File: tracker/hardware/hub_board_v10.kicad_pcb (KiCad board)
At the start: 2 copper layers, 72 x 80 mm, 28 parts, among them U1 U1, U2 U2, U3 U3, U5 U5, U6 U6, U7 U7

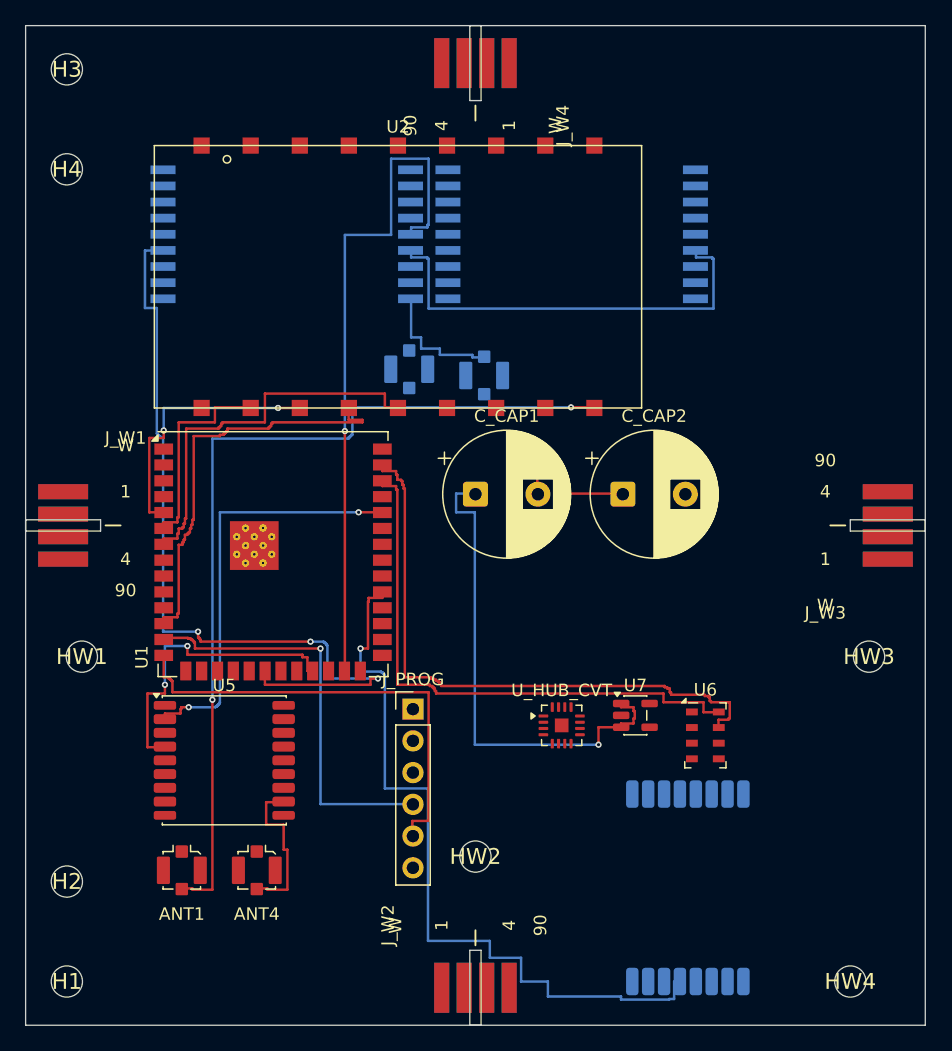
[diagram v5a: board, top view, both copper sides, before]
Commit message: fix(router): B47 -- grid marked vias 0.15mm short of the validator (consistency, NOT a win)
HONEST FRAMING: this makes the router INTERNALLY CONSISTENT. It does NOT improve the board and it
COSTS one net (19 -> 18). The board was already correct in both states -- validate_plan gates every
route, so no bad copper was ever emitted. What B47 removes is WASTED SEARCH: the grid let A* find
paths the validator then refused, which is why /U3_BUSY, /USB_DN, /GNSS_RX and /F33_RESET_N failed
with "self-check: isolation vs routed via <net> (via)" at every pitch and ordering.

THE ARITHMETIC (from validate_plan, which is the authority):
  track-vs-via  centre >= CLEAR + TRACK_W/2 + VIA_D/2 = 0.20 + 0.10 + 0.25 = 0.55mm
  via-vs-via    centre >= CLEAR + VIA_D/2   + VIA_D/2 = 0.20 + 0.25 + 0.25 = 0.70mm
Both grid-marking sites used the TRACK figure, so vias were marked 0.15mm short for the via-vs-via
case. Now marked at max(0.55, 0.70) = 0.70, so the grid can never permit what the validator refuses.
Same shape as B34/B37/B40: the grid was less strict than the check.

COST, STATED PLAINLY: a stricter grid removes detour options, so pass 2 recovered 4 nets instead of
5. 18 nets / 451 tracks / 16 vias, 9/9 custom gates rc=0, kicad-cli DRC rc=0 (0 failing,
103 unconnected). Track count rose 371 -> 451 for fewer nets because the paths now detour further.
Kept because a router whose search and validator disagree is the exact bug class that produced B34,
B37, B38, B40, B44 and B46 -- and because the discarded work made every pitch/ordering sweep
untrustworthy as a CAPACITY measurement, which is the measurement the two-layer decision needs.
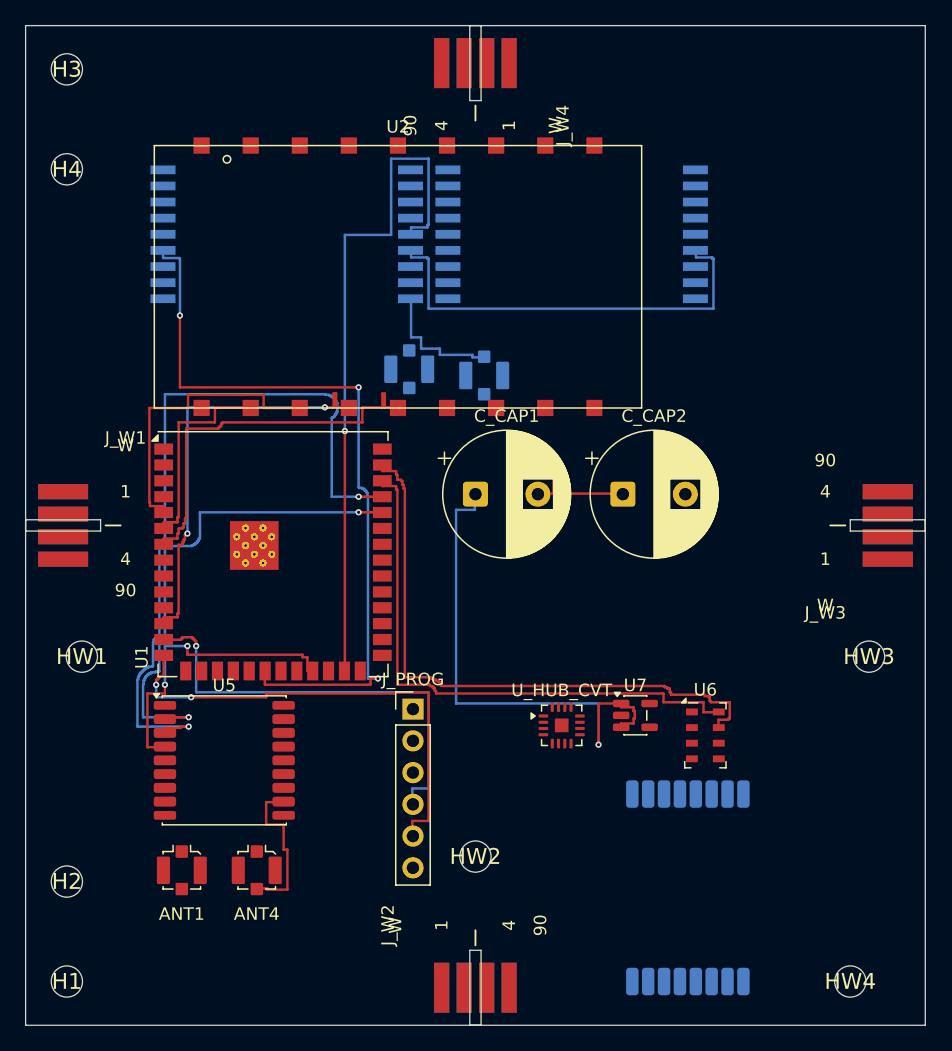
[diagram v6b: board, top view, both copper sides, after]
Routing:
- net /ANT1_433_TX: track 71.7 -> 0.00 mm, vias 2 -> 0
- net /GNSS_RX: track 0.00 -> 61.8 mm, vias 0 -> 2
- net /E28_BUSY: track 61.4 -> 0.00 mm, vias 1 -> 0
- net /GNSS_TX: track 33.9 -> 41.2 mm
- net /U3_CS_N: track 65.0 -> 62.1 mm
- net /USB_DN: track 33.4 -> 36.1 mm
- net /SPI2_MOSI: track 21.6 -> 23.7 mm, vias 2 -> 0
- net /USB_DP: track 37.0 -> 39.0 mm, vias 0 -> 2
- net /VSCAP: track 40.3 -> 42.2 mm
- net /F33_BUSY: vias 0 -> 2

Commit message: feat(v10): ADR-129 landed -- 25 refs in schematic AND board, 11/11 gates green, 3D renders ready
VERIFIED BY THE MANAGER, not relayed from the worker's self-report:
  footprints 28 -> 53 (45 parts + 8 holes); all 25 new refs present, none missing
  11/11 gates rc=0: 7 lane gates + hole_clearance + board_geometry + check_drc + schematic_parity
  check_schematic_parity  G1..G5 PASS, 58 nets agree BOTH ways, per-net pin sets equal
  kicad-cli DRC  0 failing violations (16 copper_edge_clearance + 152 silk_overlap + 28
    silk_over_copper, all three pre-existing and scoped-allowed)
  ERC 21 -> 11 errors (7 label_dangling + 2 pin_not_driven + 2 power_pin_not_driven)
  min_through_hole_diameter 0.2 preserved in the canonical .kicad_pro
  board TRACKS = 0 -- the worker did NOT route, per ADR-120 R3

TWO DEFECTS FOUND AND FIXED AFTER THE WORKER'S REPORT, both mine to catch:
1. silk_edge_clearance (NEW class, 1 item) -- "Reference field of J_HUB_PV" at x=69.0 on a 72.0mm
   board. The worker reported DRC clean but its own build introduced this. My FIRST fix GUESSED the
   text width from a per-character estimate and did not fire at all; the measured bounding box was
   (65.26,60.77)-(72.74,62.47), i.e. 0.74mm past the edge. Corrected to use
   GetBoundingBox() and shift by the MEASURED overhang -- now a general builder rule with a
   0.30mm silk-to-edge margin, so no future part can repeat it. This matters electrically only as
   assembly readability, but it is a DRC failure and DRC is the authority.
2. The ERC allowance was still 17 label_dangling after only 7 remained. An inflated allowance masks
   a regression exactly like a gate that cannot fail, so it is TIGHTENED to the measured 7 with the
   remaining seven NAMED in-source. A new dangling label now changes the count and fails the gate.

ADR-129 CLOSED TEN OF SEVENTEEN DANGLING NETS, measured:
  /F33_VCC 1->5  /GNSS_VCC 1->3  /HUB_PV_P 1->3  /HUB_PV_N 1->3  /W1_SOLAR_P 1->3
  /F33_VSENSE 1->4  /CUT_SENSE_W1..W4 1->2 e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
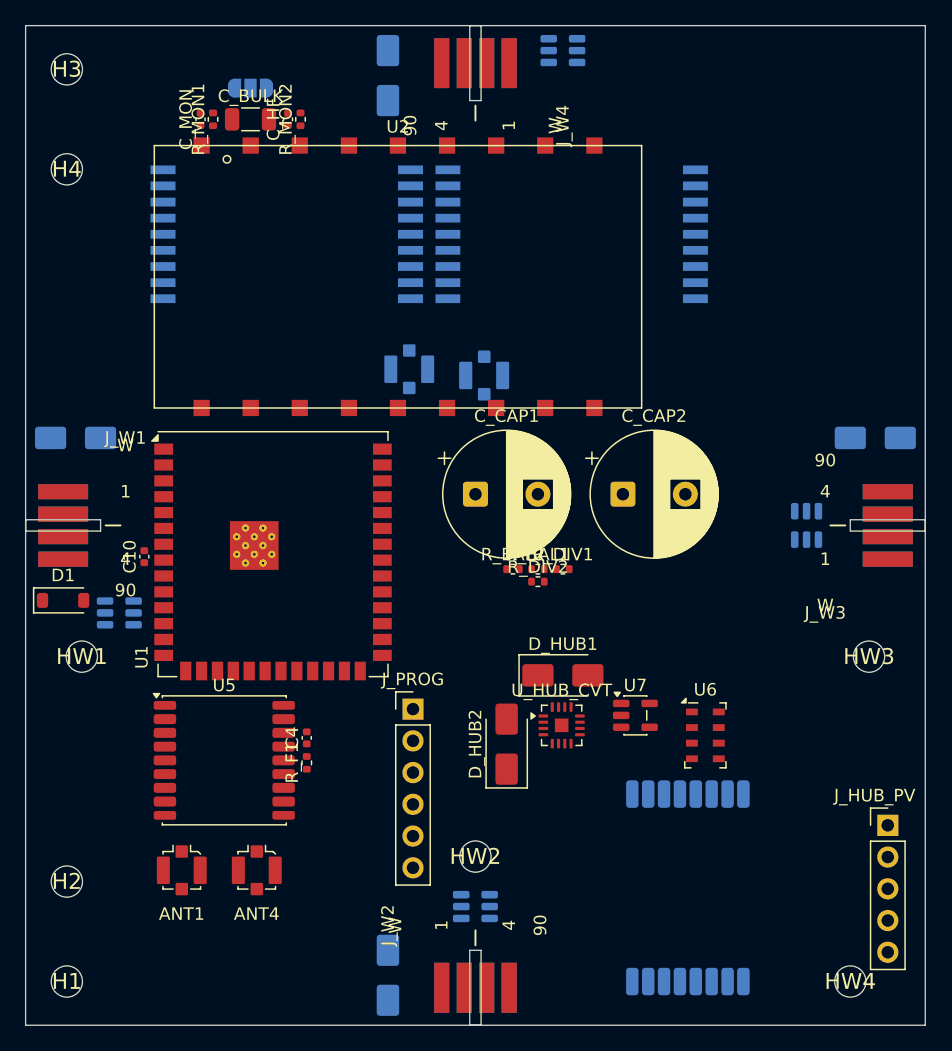
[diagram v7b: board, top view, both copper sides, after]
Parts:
- added C10: 10uF, C_0402_1005Metric, F.Cu at (9.50, 42.5)
- added C4: 10uF, C_0402_1005Metric, F.Cu at (22.5, 57.0)
- added C_BULK: 100uF, C_1206_3216Metric, F.Cu at (18.0, 7.50)
- added C_HF: 100nF, C_0402_1005Metric, F.Cu at (21.0, 7.50)
- added C_MON: 10nF, C_0402_1005Metric, F.Cu at (14.0, 7.50)
- added D1: BAT54, D_SOD-123, F.Cu at (3.00, 46.0)
- added D_BP1: SS24, D_SMA, B.Cu at (4.00, 33.0)
- added D_BP2: SS24, D_SMA, B.Cu at (29.0, 76.0)
- added D_BP3: SS24, D_SMA, B.Cu at (68.0, 33.0)
- added D_BP4: SS24, D_SMA, B.Cu at (29.0, 4.00)
- added D_HUB1: SS24, D_SMA, F.Cu at (43.0, 52.0)
- added D_HUB2: SS24, D_SMA, F.Cu at (38.5, 57.5)
- added J_HUB_PV: HUB_PV_PANEL_5P (P | MID1 | spare | N | GND), PinHeader_1x05_P2.54mm_Vertical, F.Cu at (69.0, 64.0)
- added J_VCC: F33_VCC_SEL (VSCAP | +3V3), SolderJumper-3_P1.3mm_Open_RoundedPad1.0x1.5mm, B.Cu at (18.0, 5.00)
- added R_BAL1: 10k, R_0402_1005Metric, F.Cu at (41.0, 43.5)
- added R_BAL2: 10k, R_0402_1005Metric, F.Cu at (39.0, 43.5)
- added R_DIV1: 1M, R_0402_1005Metric, F.Cu at (43.0, 43.5)
- added R_DIV2: 1M, R_0402_1005Metric, F.Cu at (41.0, 44.5)
- added R_F1: 100R, R_0402_1005Metric, F.Cu at (22.5, 59.0)
- added R_MON1: 4.7M, R_0402_1005Metric, F.Cu at (15.0, 7.50)
- added R_MON2: 4.7M, R_0402_1005Metric, F.Cu at (22.0, 7.50)
- added U_CUT1: latched cut driver + cut-sense (part TODO(unverified)), SOT-23-6, B.Cu at (7.50, 47.0)
- added U_CUT2: latched cut driver + cut-sense (part TODO(unverified)), SOT-23-6, B.Cu at (36.0, 70.5)
- added U_CUT3: latched cut driver + cut-sense (part TODO(unverified)), SOT-23-6, B.Cu at (62.5, 40.0)
- added U_CUT4: latched cut driver + cut-sense (part TODO(unverified)), SOT-23-6, B.Cu at (43.0, 2.00)
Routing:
- net /U3_CS_N: track 62.1 -> 0.00 mm, vias 3 -> 0
- net /GNSS_RX: track 61.8 -> 0.00 mm, vias 2 -> 0
- net /U3_RESET_N: track 55.2 -> 0.00 mm, vias 1 -> 0
- net /I2C_SDA: track 49.7 -> 0.00 mm
- net /I2C_SCL: track 45.4 -> 0.00 mm
- net /VSCAP: track 42.2 -> 0.00 mm, vias 1 -> 0
- net /GNSS_TX: track 41.2 -> 0.00 mm, vias 2 -> 0
- net /USB_DP: track 39.0 -> 0.00 mm, vias 2 -> 0
- net /USB_DN: track 36.1 -> 0.00 mm, vias 1 -> 0
- net /VTCXO_VNTC: track 35.0 -> 0.00 mm
- net /F33_BUSY: track 34.3 -> 0.00 mm, vias 2 -> 0
- net /F33_CS_N: track 31.9 -> 0.00 mm
- net /GNSS_PPS: track 24.7 -> 0.00 mm, vias 2 -> 0
- net /SPI2_MOSI: track 23.7 -> 0.00 mm
- net /SPI2_MISO: track 16.7 -> 0.00 mm
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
